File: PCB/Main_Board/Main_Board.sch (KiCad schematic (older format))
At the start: 18 parts, among them IC1 74LV1T34GVH, J1 USB_B_Micro, J2 Screw_Terminal_01x02, J3 SJ1-3523N, J4 SJ1-3523N, J5 Screw_Terminal_01x04, J6 Screw_Terminal_01x06, SW1 SW_SPDT, U1 TLV75533PDBV

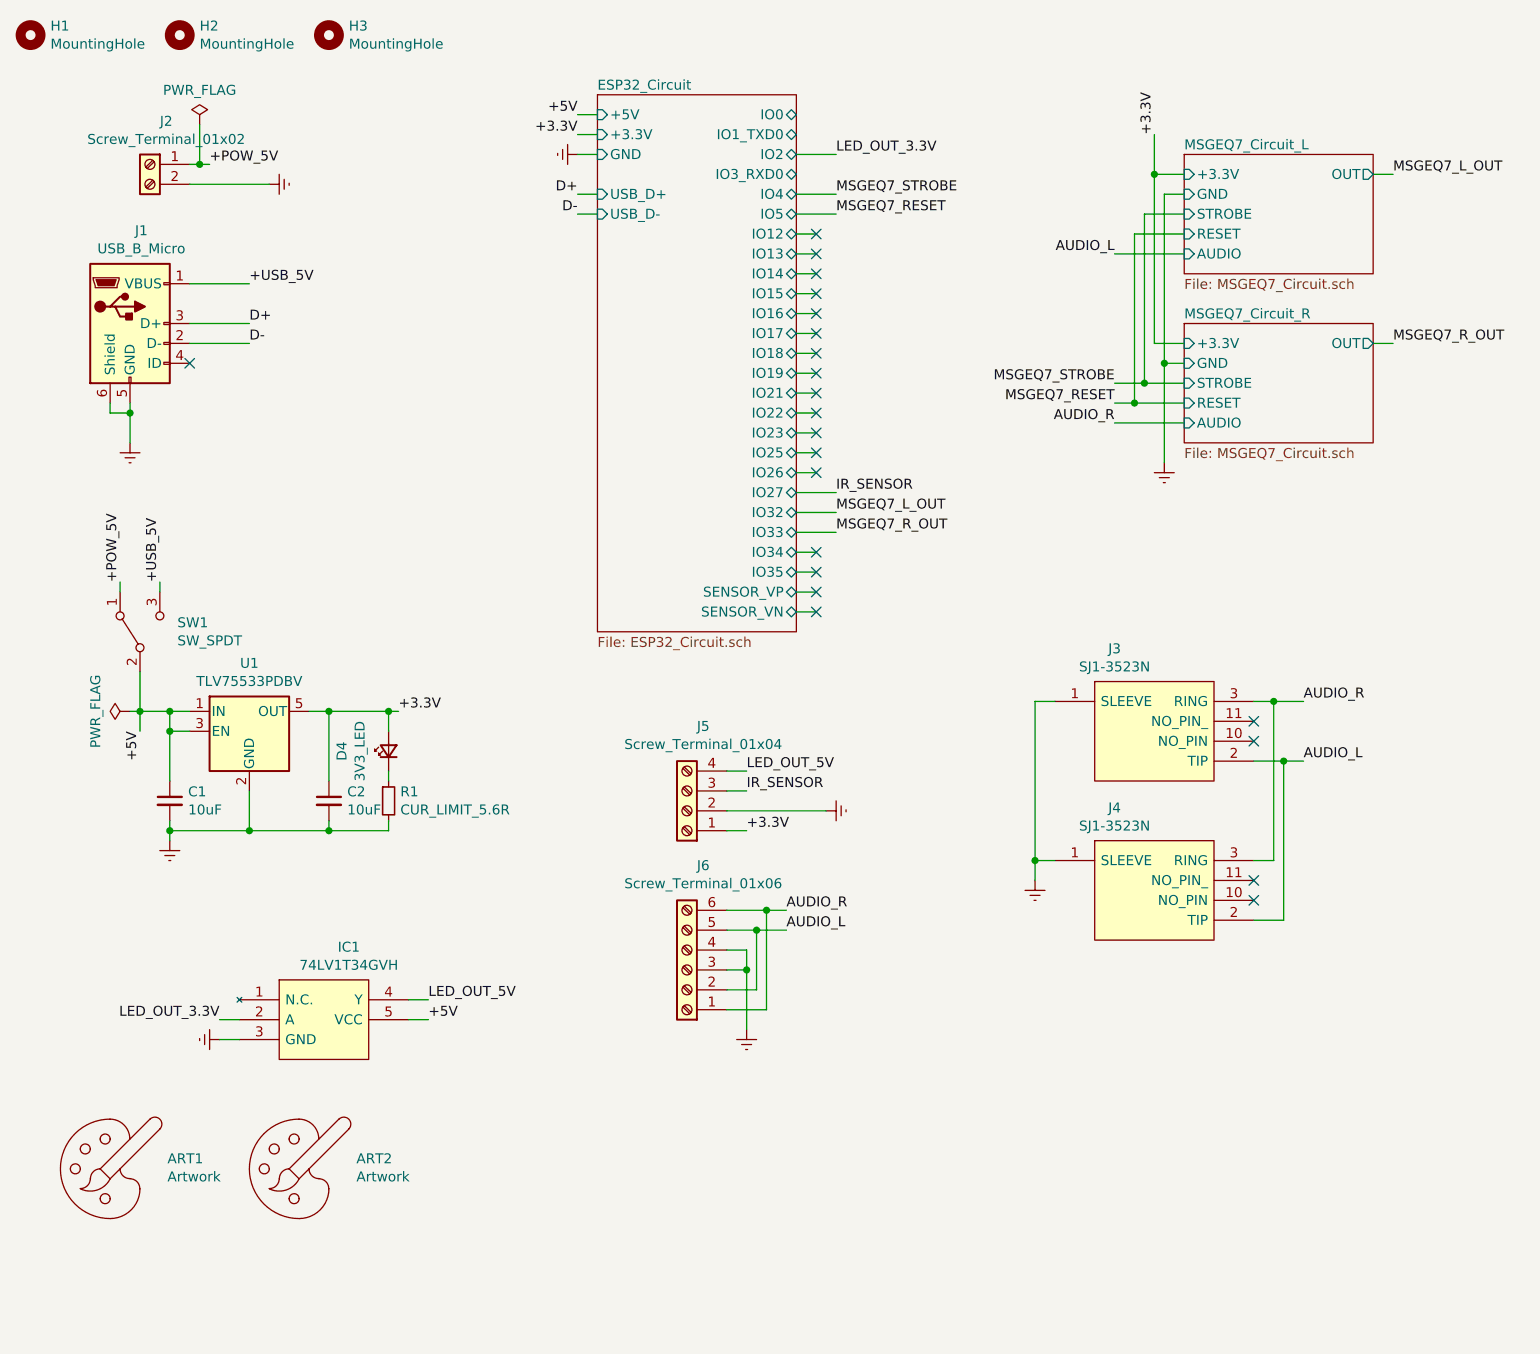
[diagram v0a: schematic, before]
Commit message: Change buttons, make board more compact, add extra mounting hole
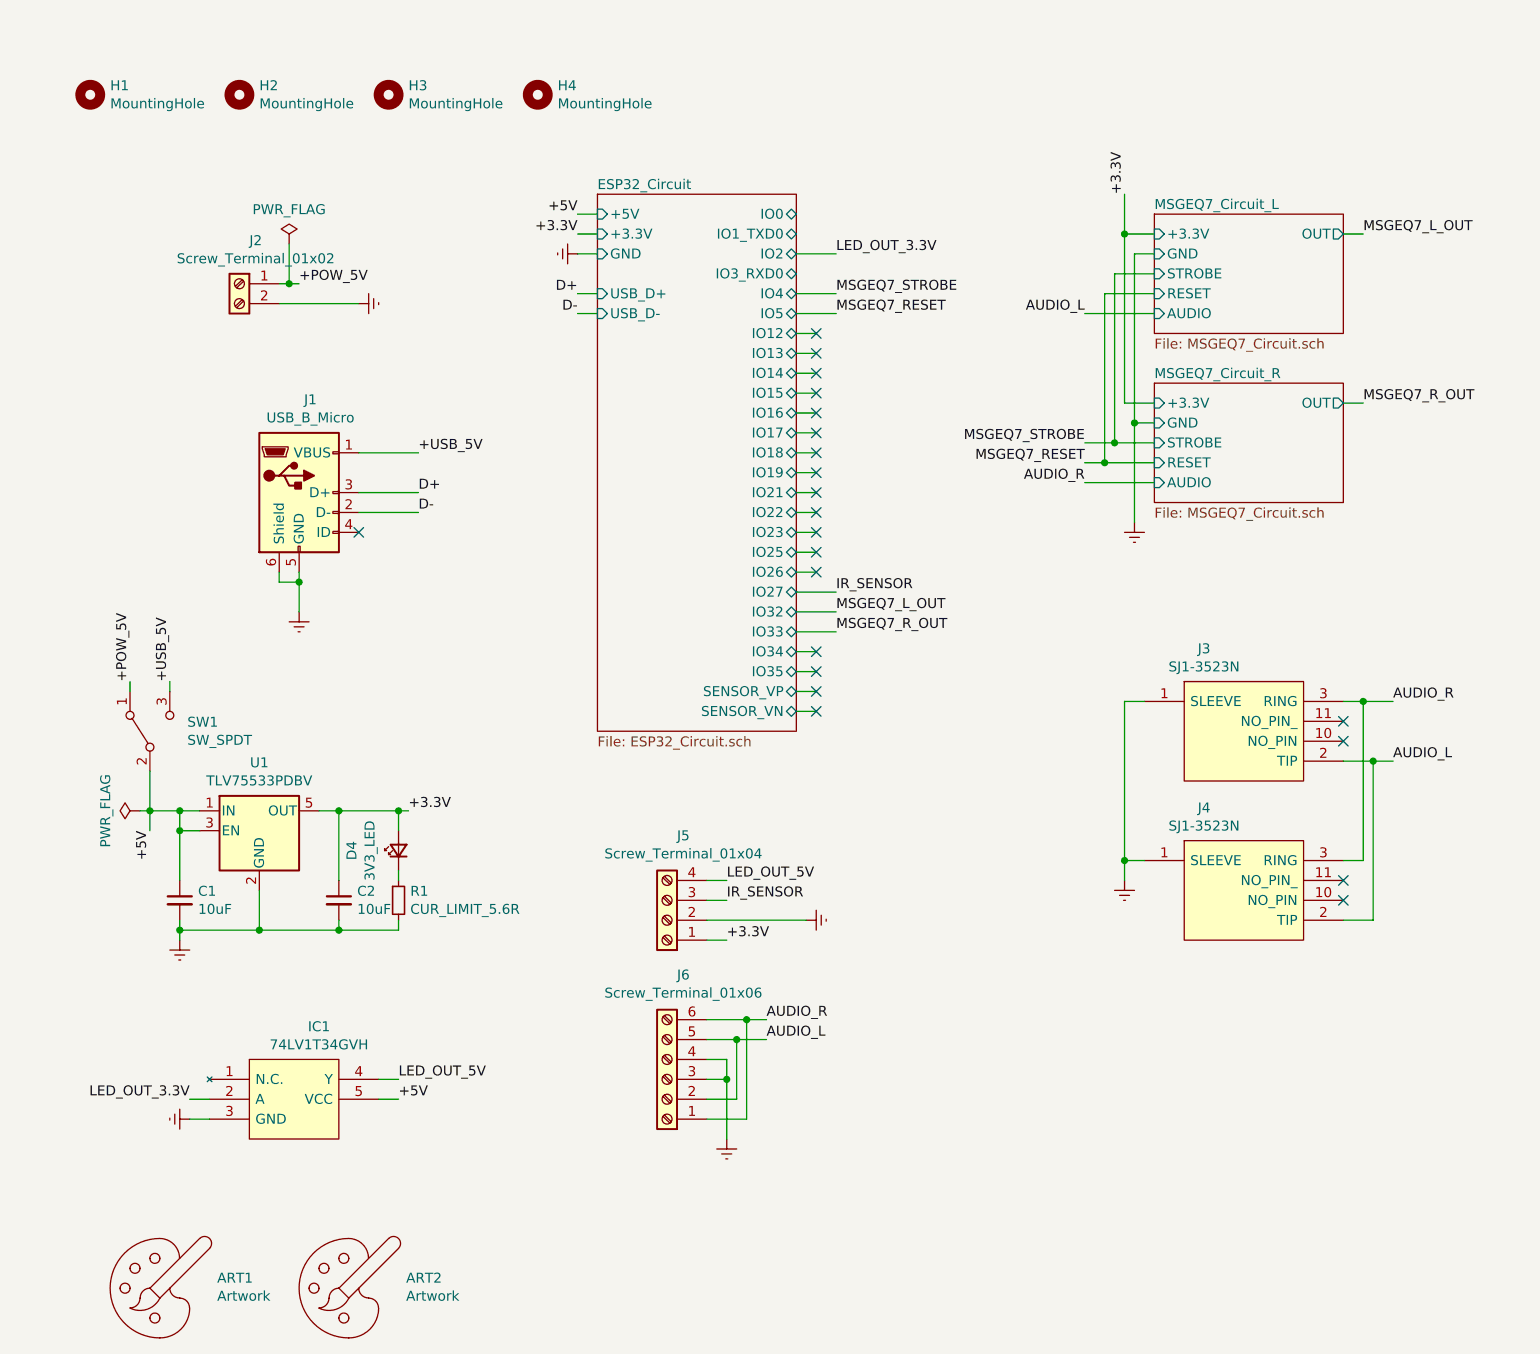
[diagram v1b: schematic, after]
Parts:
- added H4: MountingHole, MountingHole:MountingHole_3.2mm_M3, symbol Mechanical:MountingHole
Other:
- moved on the sheet: ART1, ART2, C1, C2, D4, H1, H2, H3, IC1, J1, J2, J3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

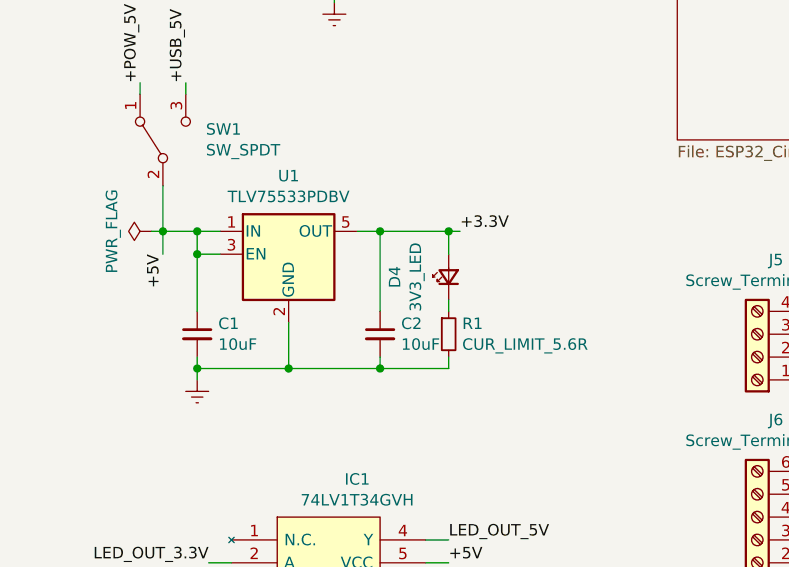
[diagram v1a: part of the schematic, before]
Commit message: Move indicator LED to 5V and increase indicator LED resistors
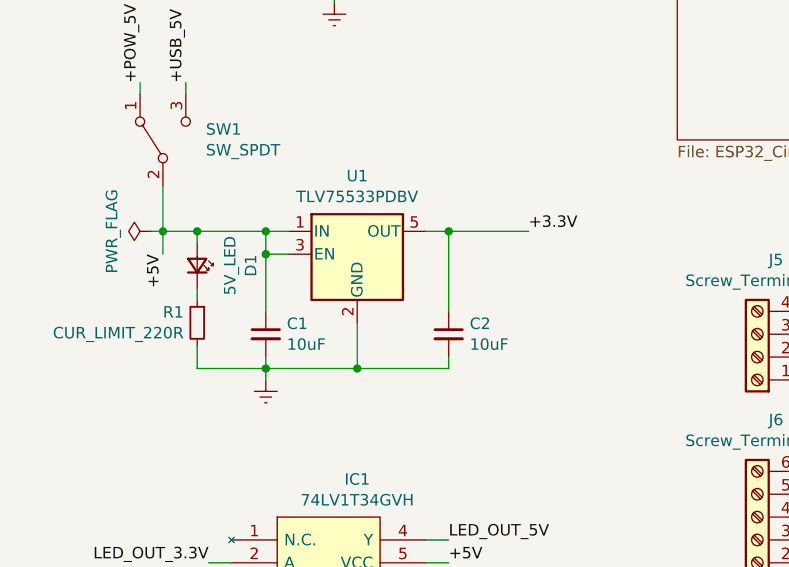
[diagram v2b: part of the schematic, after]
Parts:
- removed D4: 3V3_LED, LED_SMD:LED_0603_1608Metric_Pad1.05x0.95mm_HandSolder, symbol Device:LED_Small
- added D1: 5V_LED, LED_SMD:LED_0603_1608Metric_Pad1.05x0.95mm_HandSolder, symbol Device:LED_Small
- R1: value CUR_LIMIT_5.6R -> CUR_LIMIT_220R
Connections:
- net +5V: now also D1.2 (A)
- net at R1.1: now also D1.1 (K)
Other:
- moved on the sheet: C1, C2, U1
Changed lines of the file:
@@
 	4050 5100 4550 5100
 Wire Wire Line
-	1800 5150 2200 5150
-Connection ~ 1800 5150
-Wire Wire Line
-	1800 4950 1800 5150
-Wire Wire Line
-	2200 5150 2200 5100
-Wire Wire Line
-	1400 5150 1800 5150
-Wire Wire Line
-	1400 5100 1400 5150
-Wire Wire Line
-	1400 4650 1400 4550
-Connection ~ 1400 4650
-Wire Wire Line
-	1500 4650 1400 4650
-Wire Wire Line
-	1400 4550 1500 4550
-Wire Wire Line
-	1400 4900 1400 4650
+	2100 5150 2500 5150
+Connection ~ 2100 5150
+Wire Wire Line
+	2100 4950 2100 5150
+Wire Wire Line
+	2500 5150 2500 5100
+Wire Wire Line
+	1700 5150 2100 5150
+Wire Wire Line
+	1700 5100 1700 5150
+Wire Wire Line
+	1700 4650 1700 4550
+Connection ~ 1700 4650
+Wire Wire Line
+	1800 4650 1700 4650
+Wire Wire Line
+	1700 4550 1800 4550
+Wire Wire Line
+	1700 4900 1700 4650
 $Comp
 L Regulator_Linear:TLV75533PDBV U1
 U 1 1 5F884D3D
-P 1800 4650
+P 2100 4650
 AR Path="/5F884D3D" Ref="U1"  Part="1"
 AR Path="/5F591C5D/5F884D3D" Ref="U?"  Part="1"
-F 0 "U1" H 1800 4992 50  0000 C CNN
-F 1 "TLV75533PDBV" H 1800 4901 50  0000 C CNN
-F 2 "Package_TO_SOT_SMD:SOT-23-5" H 1800 4975 50  0001 C CIN
-F 3 "http://www.ti.com/lit/ds/symlink/tlv755p.pdf" H 1800 4700 50  0001 C CNN
-	1    1800 4650
+F 0 "U1" H 2100 4992 50  0000 C CNN
+F 1 "TLV75533PDBV" H 2100 4901 50  0000 C CNN
+F 2 "Package_TO_SOT_SMD:SOT-23-5" H 2100 4975 50  0001 C CIN
+F 3 "http://www.ti.com/lit/ds/symlink/tlv755p.pdf" H 2100 4700 50  0001 C CNN
+	1    2100 4650
 	1    0    0    -1
 $EndComp
 Wire Wire Line
-	2200 4550 2100 4550
-Wire Wire Line
-	2200 4900 2200 4550
+	2500 4550 2400 4550
+Wire Wire Line
+	2500 4900 2500 4550
 Wire Wire Line
 	1250 4350 1250 4550
-Wire Wire Line
-	1250 4550 1400 4550
-Connection ~ 1400 4550
 $Comp
 L power:Earth #PWR02
 U 1 1 5F884D4E
-P 1400 5200
+P 1700 5200
 AR Path="/5F884D4E" Ref="#PWR02"  Part="1"
 AR Path="/5F591C5D/5F884D4E" Ref="#PWR?"  Part="1"
-F 0 "#PWR02" H 1400 4950 50  0001 C CNN
-F 1 "Earth" H 1400 5050 50  0001 C CNN
-F 2 "" H 1400 5200 50  0001 C CNN
-F 3 "~" H 1400 5200 50  0001 C CNN
-	1    1400 5200
+F 0 "#PWR02" H 1700 4950 50  0001 C CNN
+F 1 "Earth" H 1700 5050 50  0001 C CNN
+F 2 "" H 1700 5200 50  0001 C CNN
+F 3 "~" H 1700 5200 50  0001 C CNN
+	1    1700 5200
 	1    0    0    -1
 $EndComp
 Wire Wire Line
-	1400 5200 1400 5150
-Connection ~ 1400 5150
-$Comp
-L Device:LED_Small D4
-U 1 1 5F884D56
-P 2500 4750
-AR Path="/5F884D56" Ref="D4"  Part="1"
-AR Path="/5F591C5D/5F884D56" Ref="D?"  Part="1"
-F 0 "D4" H 2500 4985 50  0000 C CNN
-F 1 "3V3_LED" H 2500 4894 50  0000 C CNN
-F 2 "LED_SMD:LED_0603_1608Metric_Pad1.05x0.95mm_HandSolder" V 2500 4750 50  0001 C CNN
-F 3 "~" V 2500 4750 50  0001 C CNN
-	1    2500 4750
-	0    -1   -1   0
-$EndComp
-$Comp
-L Device:R_Small R1
-U 1 1 5F884D5C
-P 2500 5000
-AR Path="/5F884D5C" Ref="R1"  Part="1"
-AR Path="/5F591C5D/5F884D5C" Ref="R?"  Part="1"
-F 0 "R1" H 2559 5046 50  0000 L CNN
-F 1 "CUR_LIMIT_5.6R" H 2559 4955 50  0000 L CNN
-F 2 "Resistor_SMD:R_0603_1608Metric_Pad1.05x0.95mm_HandSolder" H 2500 5000 50  0001 C CNN
-F 3 "~" H 2500 5000 50  0001 C CNN
-	1    2500 5000
-	1    0    0    -1
-$EndComp
-Wire Wire Line
-	2200 4550 2500 4550
-Wire Wire Line
-	2500 4550 2500 4650
-Connection ~ 2200 4550
-Wire Wire Line
-	2500 5100 2500 5150
-Wire Wire Line
-	2500 5150 2200 5150
-Connection ~ 2200 5150
-Wire Wire Line
-	2500 4850 2500 4900
-Wire Wire Line
-	2500 4550 2550 4550
+	1700 5200 1700 5150
+Connection ~ 1700 5150
 Connection ~ 2500 4550
 $Comp
@@
 Text Label 1150 3900 1    50   ~ 0
 +POW_5V
-Text Label 2550 4550 0    50   ~ 0
+Text Label 2850 4550 0    50   ~ 0
 +3.3V
 $Comp
@@
 L Device:C_Small C1
 U 1 1 5F96B41D
-P 1400 5000
+P 1700 5000
 AR Path="/5F96B41D" Ref="C1"  Part="1"
 AR Path="/5F591C5D/5F96B41D" Ref="C?"  Part="1"
 AR Path="/5F889015/5F96B41D" Ref="C?"  Part="1"
-F 0 "C1" H 1492 5046 50  0000 L CNN
-F 1 "10uF" H 1492 4955 50  0000 L CNN
-F 2 "Capacitor_SMD:C_0603_1608Metric_Pad1.05x0.95mm_HandSolder" H 1400 5000 50  0001 C CNN
-F 3 "~" H 1400 5000 50  0001 C CNN
-	1    1400 5000
+F 0 "C1" H 1792 5046 50  0000 L CNN
+F 1 "10uF" H 1792 4955 50  0000 L CNN
+F 2 "Capacitor_SMD:C_0603_1608Metric_Pad1.05x0.95mm_HandSolder" H 1700 5000 50  0001 C CNN
+F 3 "~" H 1700 5000 50  0001 C CNN
+	1    1700 5000
 	1    0    0    -1
 $EndComp
@@
 L Device:C_Small C2
 U 1 1 5F9710DE
-P 2200 5000
+P 2500 5000
 AR Path="/5F9710DE" Ref="C2"  Part="1"
 AR Path="/5F591C5D/5F9710DE" Ref="C?"  Part="1"
 AR Path="/5F889015/5F9710DE" Ref="C?"  Part="1"
-F 0 "C2" H 2292 5046 50  0000 L CNN
-F 1 "10uF" H 2292 4955 50  0000 L CNN
-F 2 "Capacitor_SMD:C_0603_1608Metric_Pad1.05x0.95mm_HandSolder" H 2200 5000 50  0001 C CNN
-F 3 "~" H 2200 5000 50  0001 C CNN
-	1    2200 5000
+F 0 "C2" H 2592 5046 50  0000 L CNN
+F 1 "10uF" H 2592 4955 50  0000 L CNN
+F 2 "Capacitor_SMD:C_0603_1608Metric_Pad1.05x0.95mm_HandSolder" H 2500 5000 50  0001 C CNN
+F 3 "~" H 2500 5000 50  0001 C CNN
+	1    2500 5000
 	1    0    0    -1
 $EndComp
@@
 Wire Wire Line
 	4500 3450 4700 3450
+Connection ~ 1700 4550
+Wire Wire Line
+	1400 4600 1400 4550
+Wire Wire Line
+	1400 5050 1400 5150
+$Comp
+L Device:R_Small R1
+U 1 1 5F6DD4EB
+P 1400 4950
+AR Path="/5F6DD4EB" Ref="R1"  Part="1"
+AR Path="/5F591C5D/5F6DD4EB" Ref="R?"  Part="1"
+F 0 "R1" H 1459 4996 50  0000 L CNN
+F 1 "CUR_LIMIT_220R" H 1459 4905 50  0000 L CNN
+F 2 "Resistor_SMD:R_0603_1608Metric_Pad1.05x0.95mm_HandSolder" H 1400 4950 50  0001 C CNN
+F 3 "~" H 1400 4950 50  0001 C CNN
+	1    1400 4950
+	-1   0    0    -1
+$EndComp
+Wire Wire Line
+	1400 4800 1400 4850
+$Comp
+L Device:LED_Small D1
+U 1 1 5F6DD4E4
+P 1400 4700
+AR Path="/5F6DD4E4" Ref="D1"  Part="1"
+AR Path="/5F591C5D/5F6DD4E4" Ref="D?"  Part="1"
+F 0 "D1" H 1400 4935 50  0000 C CNN
+F 1 "5V_LED" H 1400 4844 50  0000 C CNN
+F 2 "LED_SMD:LED_0603_1608Metric_Pad1.05x0.95mm_HandSolder" V 1400 4700 50  0001 C CNN
+F 3 "~" V 1400 4700 50  0001 C CNN
+	1    1400 4700
+	0    1    -1   0
+$EndComp
+Wire Wire Line
+	1250 4550 1400 4550
+Connection ~ 1400 4550
+Wire Wire Line
+	1400 4550 1700 4550
+Wire Wire Line
+	1400 5150 1700 5150
+Wire Wire Line
+	2500 4550 2850 4550
 $EndSCHEMATC

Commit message: Update KiCAD to 5.1.7 and change a couple of footprints
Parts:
- J2: footprint TerminalBlock:TerminalBlock_bornier-2_P5.08mm -> Missing_Models:TerminalBlock_bornier-2_P5.08mm
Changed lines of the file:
@@
 F 0 "J2" H 1618 2117 50  0000 C CNN
 F 1 "Screw_Terminal_01x02" H 1618 2026 50  0000 C CNN
-F 2 "TerminalBlock:TerminalBlock_bornier-2_P5.08mm" H 1700 1900 50  0001 C CNN
+F 2 "Missing_Models:TerminalBlock_bornier-2_P5.08mm" H 1700 1900 50  0001 C CNN
 F 3 "~" H 1700 1900 50  0001 C CNN
 F 4 "https://www.mouser.co.uk/ProductDetail/CUI-Devices/TB006-508-02BE?qs=vLWxofP3U2wEdOVV%2FaT04w%3D%3D" H 1700 1900 50  0001 C CNN "Product"
